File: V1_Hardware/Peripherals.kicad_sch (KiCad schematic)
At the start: 11 parts, among them U6 BMI088, U7 BMP388, U8 LIS3MDL

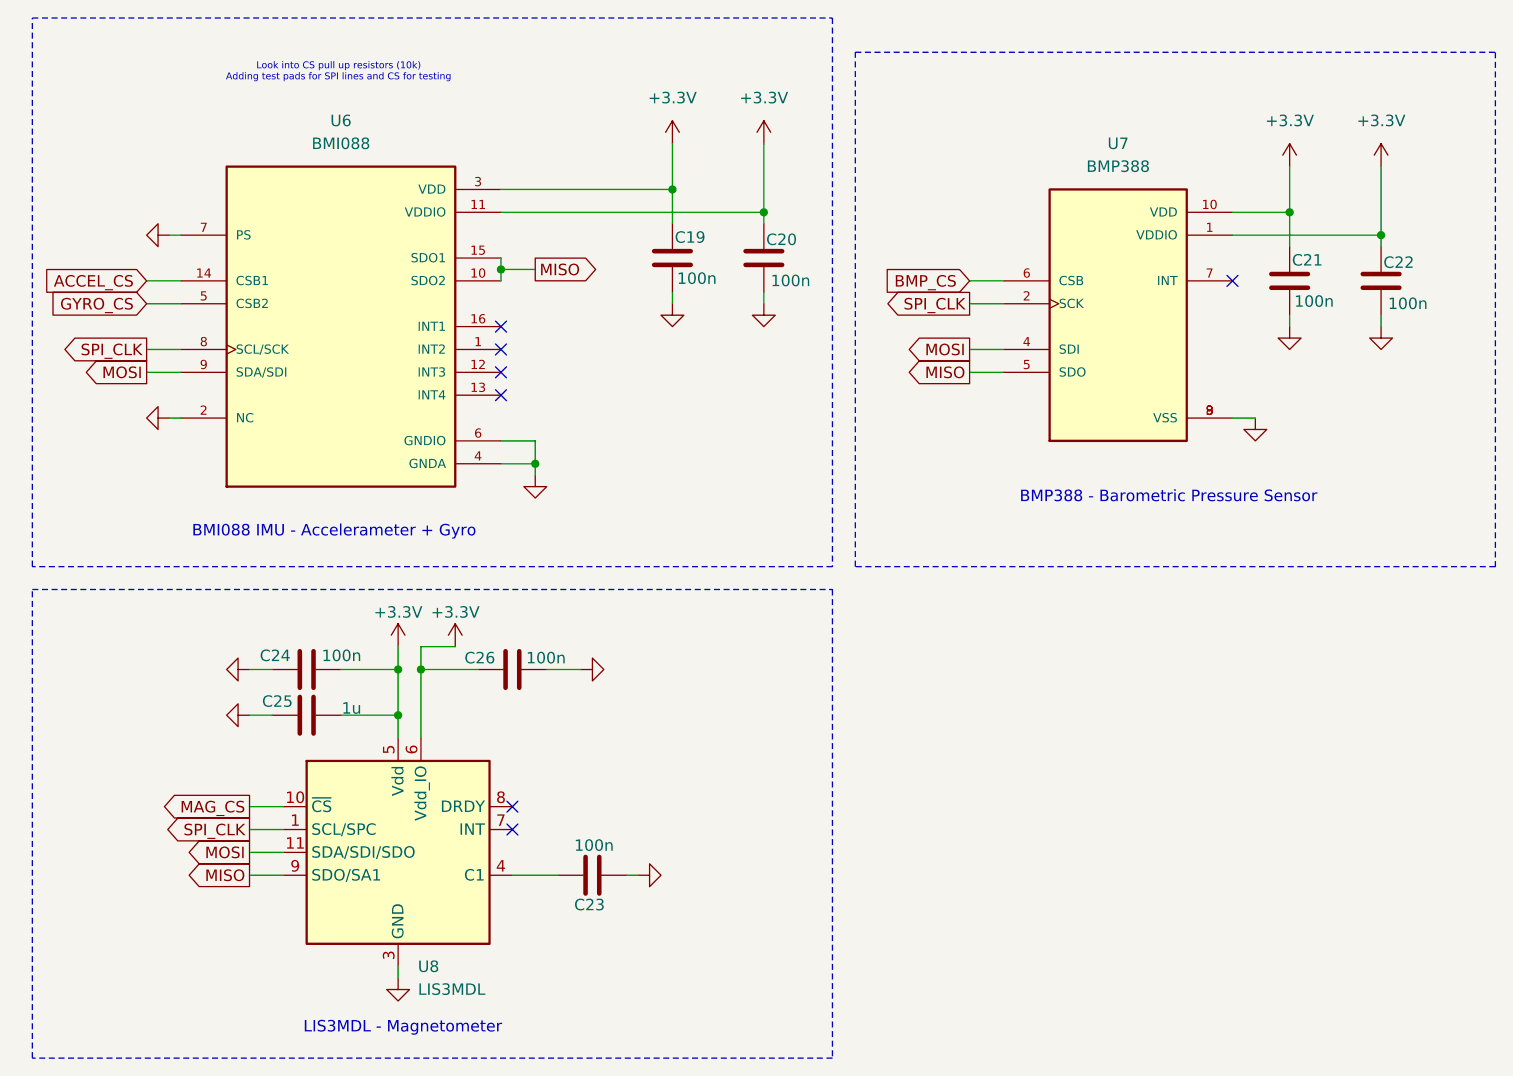
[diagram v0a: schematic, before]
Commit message: added the V1 to personal repo from org repo
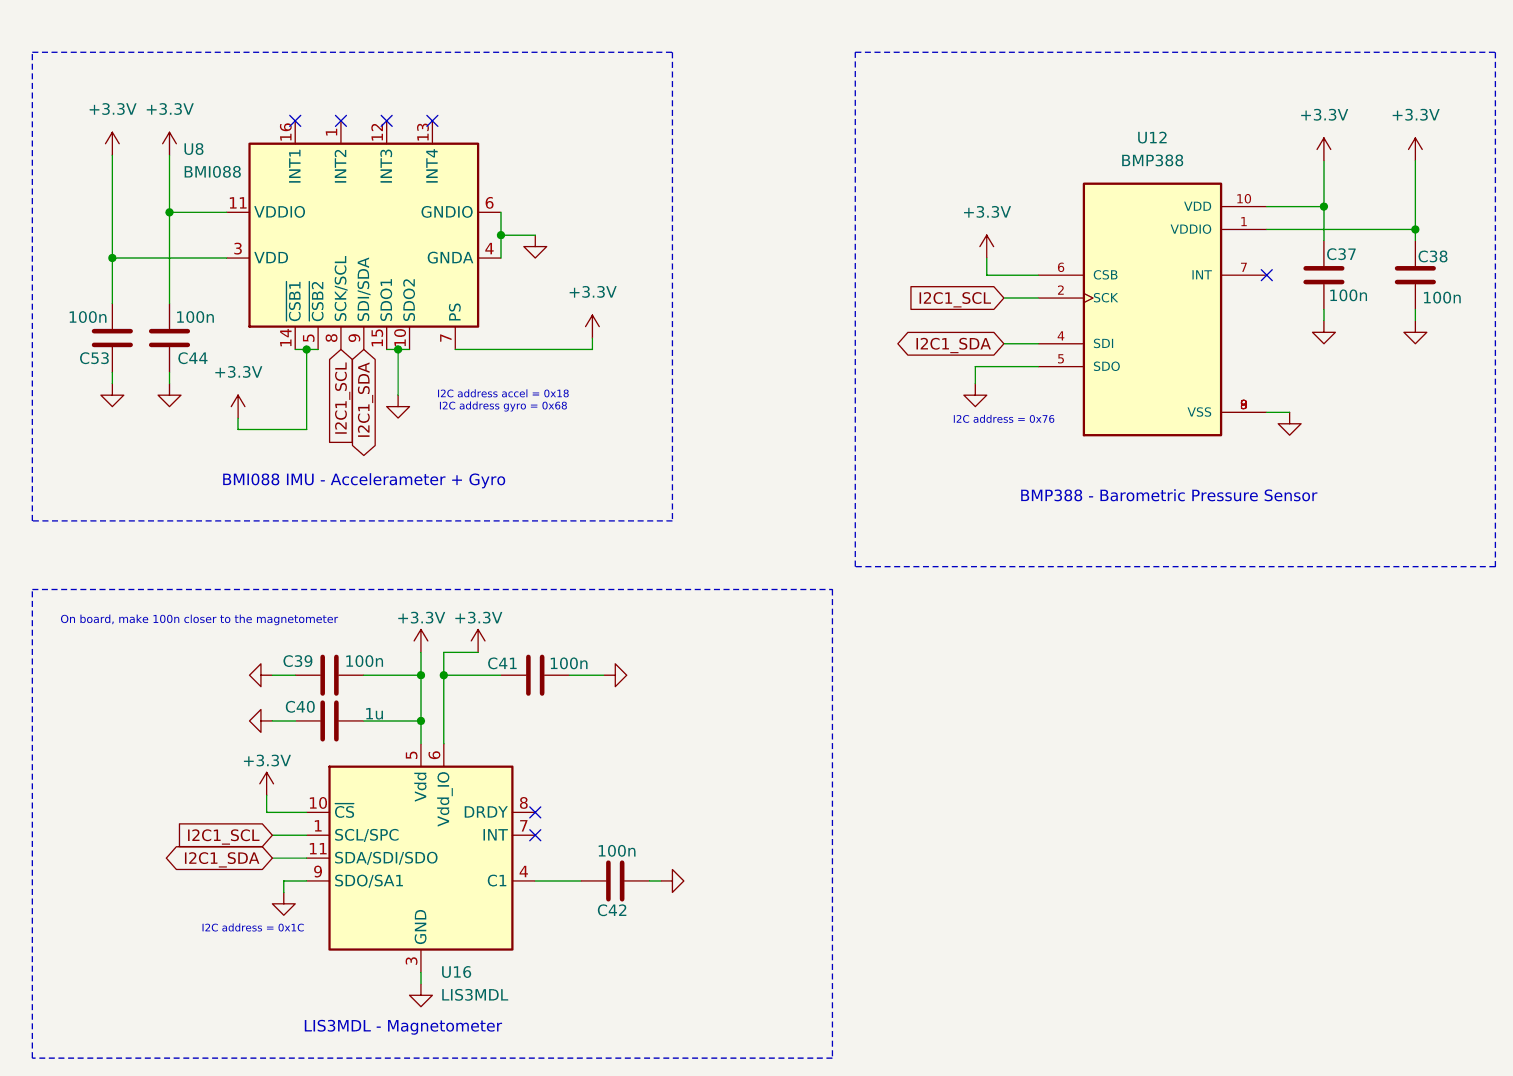
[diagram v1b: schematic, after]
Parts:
- removed C19, C20, C21, C22, C23, C24, C26: 100n, symbol Device:C
- removed C25: 1u, symbol Device:C
- removed U6: BMI088, BMI088:PQFN50P450X300X100-16N, symbol BMI088:BMI088
- removed U7: BMP388, BMP388:PQFN50P200X200X80-10N, symbol BMP388:BMP388
- removed U8: LIS3MDL, Package_LGA:LGA-12_2x2mm_P0.5mm, symbol Sensor_Magnetic:LIS3MDL
- added C37, C38, C39, C41, C42, C44, C53: 100n, Capacitor_SMD:C_0603_1608Metric_Pad1.08x0.95mm_HandSolder, symbol Device:C
- added C40: 1u, Capacitor_SMD:C_0603_1608Metric_Pad1.08x0.95mm_HandSolder, symbol Device:C
- added U12: BMP388, V1:BMP388, symbol BMP388:BMP388
- added U16: LIS3MDL, Package_LGA:LGA-12_2x2mm_P0.5mm, symbol Sensor_Magnetic:LIS3MDL
- added U8: BMI088, Package_LGA:Bosch_LGA-16_4.5x3mm_P0.5mm_LayoutBorder7x1y_ClockwisePinNumbering, symbol Sensor_Motion:BMI088
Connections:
- net +3.3V: now also C37.1, C38.1, C39.2, C40.2, C41.2, C44.2, C53.2, U12.1 (VDDIO), U12.10 (VDD), U12.6 (CSB), U16.10 (~{CS}), U16.5 (Vdd), U16.6 (Vdd_IO), U8.11 (VDDIO), U8.14 (~{CSB1}), U8.3 (VDD), U8.5 (~{CSB2}), U8.7 (PS)
- net GND: now also C37.2, C38.2, C39.1, C40.1, C41.1, C42.1, C44.1, C53.1, U12.3 (VSS), U12.5 (SDO), U12.8 (VSS), U12.9 (VSS), U16.12 (GND), U16.2 (GND), U16.3 (GND), U16.9 (SDO/SA1), U8.10 (SDO2), U8.15 (SDO1), U8.2 (GNDA), U8.4 (GNDA), U8.6 (GNDIO)
- new net: C42.2, U16.4 (C1)
- new net I2C1_SCL: U12.2 (SCK), U16.1 (SCL/SPC), U8.8 (SCK/SCL)
- new net I2C1_SDA: U12.4 (SDI), U16.11 (SDA/SDI/SDO), U8.9 (SDI/SDA)
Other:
- note added: "I2C address = 0x1C"
- note added: "I2C address = 0x76"
- note added: "I2C address accel = 0x18 I2C address gyro = 0x68"
- note added: "On board, make 100n closer to the magnetometer"
- note removed: "Look into CS pull up resistors (10k) Adding test pads for SPI lines and CS for testing"
